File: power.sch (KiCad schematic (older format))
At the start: 0 parts

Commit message: Power
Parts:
- added C? (x2): C, ~, symbol C
- added F? (x4): FUSE, ~, symbol FUSE
- added L? (x2): INDUCTOR, ~, symbol INDUCTOR
- added P?: CONN_12X2, symbol CONN_12X2
- added R?: R, ~, symbol R
- added SW?: SWITCH_INV, ~, symbol SWITCH_INV
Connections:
- new net: F?.1, P?.10 (P10)
- new net: F?.1, P?.14 (P14)
- new net: P?.16 (P16), SW?.2
- new net: F?.1, P?.2 (P2)
- new net: F?.1, P?.4 (P4), P?.6 (P6)
- new net: R?.1, SW?.1
- new net +12P: F?.2, L?.1
- new net +12V: C?.1, L?.2
- new net +3.3V: F?.2, R?.2
- new net +5V: F?.2
- new net -12P: F?.2, L?.1
- new net -12V: C?.2, L?.2
- new net GND: C?.1, C?.2, P?.3 (P3), P?.5 (P5), SW?.3

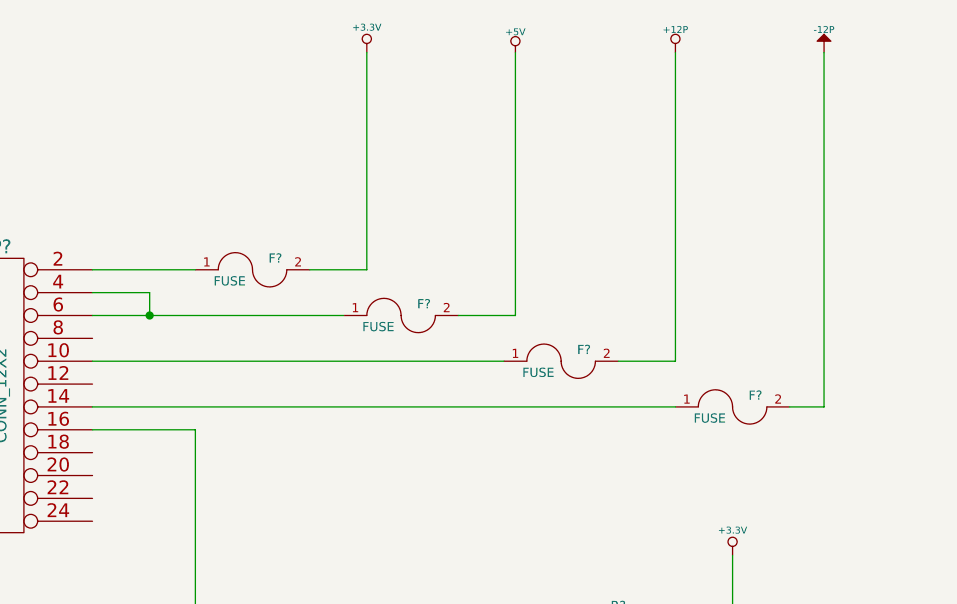
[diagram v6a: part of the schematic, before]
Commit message: Fan/Power refactoring
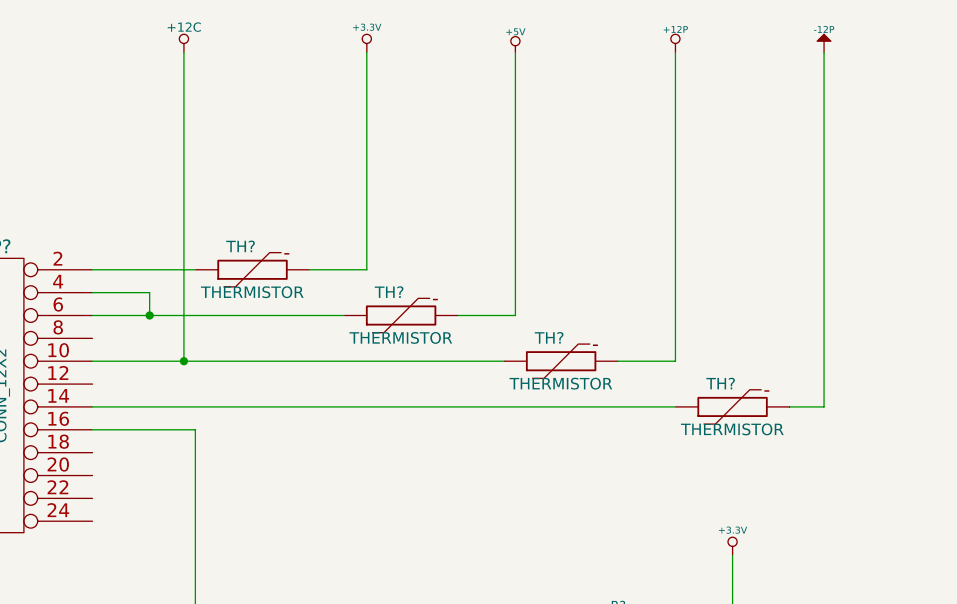
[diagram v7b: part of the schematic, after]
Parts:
- removed F? (x4): FUSE, ~, symbol FUSE
- added TH? (x4): THERMISTOR, ~, symbol THERMISTOR
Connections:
- net +12P: now also TH?.2
- net +3.3V: now also TH?.2
- net +5V: now also TH?.2
- net -12P: now also TH?.2
- net +12C: now reaches P?.10 (P10)
- net +12C: now also TH?.1
- net at P?.14 (P14): now also TH?.1
- net at P?.2 (P2): now also TH?.1
- net at P?.4 (P4), P?.6 (P6): now also TH?.1
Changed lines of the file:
@@
-$EndComp
-$Comp
-L FUSE F?
-U 1 1 52F4AFDE
-P 3950 1950
-F 0 "F?" H 4050 2000 40  0000 C CNN
-F 1 "FUSE" H 3850 1900 40  0000 C CNN
-F 2 "~" H 3950 1950 60  0000 C CNN
-F 3 "~" H 3950 1950 60  0000 C CNN
-	1    3950 1950
-	1    0    0    -1
-$EndComp
-$Comp
-L FUSE F?
-U 1 1 52F4AFED
-P 4600 2150
-F 0 "F?" H 4700 2200 40  0000 C CNN
-F 1 "FUSE" H 4500 2100 40  0000 C CNN
-F 2 "~" H 4600 2150 60  0000 C CNN
-F 3 "~" H 4600 2150 60  0000 C CNN
-	1    4600 2150
-	1    0    0    -1
-$EndComp
-$Comp
-L FUSE F?
-U 1 1 52F4AFFC
-P 5300 2350
-F 0 "F?" H 5400 2400 40  0000 C CNN
-F 1 "FUSE" H 5200 2300 40  0000 C CNN
-F 2 "~" H 5300 2350 60  0000 C CNN
-F 3 "~" H 5300 2350 60  0000 C CNN
-	1    5300 2350
-	1    0    0    -1
-$EndComp
-$Comp
-L FUSE F?
-U 1 1 52F4B00B
-P 6050 2550
-F 0 "F?" H 6150 2600 40  0000 C CNN
-F 1 "FUSE" H 5950 2500 40  0000 C CNN
-F 2 "~" H 6050 2550 60  0000 C CNN
-F 3 "~" H 6050 2550 60  0000 C CNN
-	1    6050 2550
-	1    0    0    -1
 $EndComp
 $Comp
@@
 	1950 2150 1950 2050
 Connection ~ 1950 2050
+$Comp
+L +12C #PWR?
+U 1 1 52F6562A
+P 3650 1000
+F 0 "#PWR?" H 3650 970 30  0001 C CNN
+F 1 "+12C" H 3650 1110 40  0000 C CNN
+F 2 "" H 3650 1000 60  0000 C CNN
+F 3 "" H 3650 1000 60  0000 C CNN
+	1    3650 1000
+	1    0    0    -1
+$EndComp
+Wire Wire Line
+	3650 1000 3650 2350
+Connection ~ 3650 2350
+$Comp
+L THERMISTOR TH?
+U 1 1 52F65EBA
+P 3950 1950
+F 0 "TH?" V 4050 2000 50  0000 C CNN
+F 1 "THERMISTOR" V 3850 1950 50  0000 C CNN
+F 2 "~" H 3950 1950 60  0000 C CNN
+F 3 "~" H 3950 1950 60  0000 C CNN
+	1    3950 1950
+	0    -1   -1   0
+$EndComp
+$Comp
+L THERMISTOR TH?
+U 1 1 52F65EC9
+P 4600 2150
+F 0 "TH?" V 4700 2200 50  0000 C CNN
+F 1 "THERMISTOR" V 4500 2150 50  0000 C CNN
+F 2 "~" H 4600 2150 60  0000 C CNN
+F 3 "~" H 4600 2150 60  0000 C CNN
+	1    4600 2150
+	0    -1   -1   0
+$EndComp
+$Comp
+L THERMISTOR TH?
+U 1 1 52F65ED8
+P 5300 2350
+F 0 "TH?" V 5400 2400 50  0000 C CNN
+F 1 "THERMISTOR" V 5200 2350 50  0000 C CNN
+F 2 "~" H 5300 2350 60  0000 C CNN
+F 3 "~" H 5300 2350 60  0000 C CNN
+	1    5300 2350
+	0    -1   -1   0
+$EndComp
+$Comp
+L THERMISTOR TH?
+U 1 1 52F65EE7
+P 6050 2550
+F 0 "TH?" V 6150 2600 50  0000 C CNN
+F 1 "THERMISTOR" V 5950 2550 50  0000 C CNN
+F 2 "~" H 6050 2550 60  0000 C CNN
+F 3 "~" H 6050 2550 60  0000 C CNN
+	1    6050 2550
+	0    -1   -1   0
+$EndComp
 $EndSCHEMATC
